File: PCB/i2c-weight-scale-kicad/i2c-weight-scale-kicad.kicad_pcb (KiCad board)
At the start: 2 copper layers, 43 x 49 mm, 13 parts, among them J1 I2C_RJ14, P1 4_STRAIN_GAUGES, U1 INA126, U2 PIC12F1822

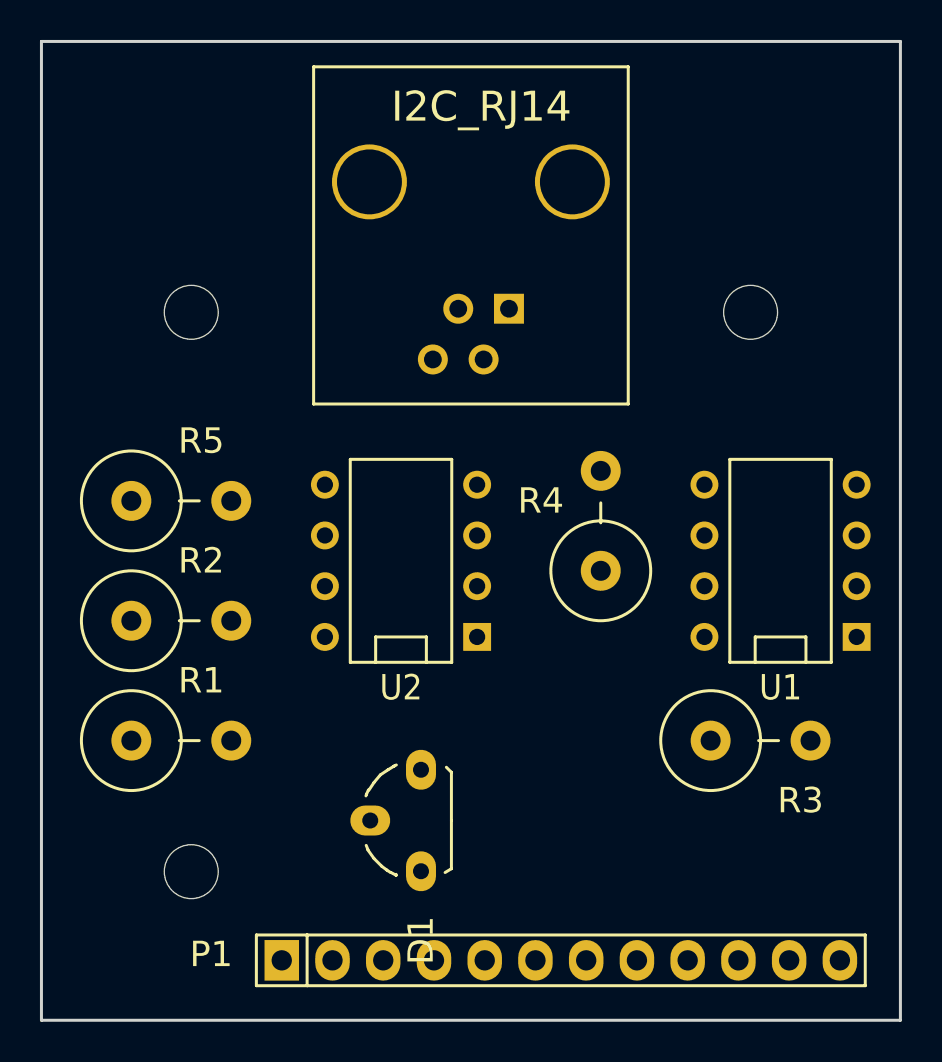
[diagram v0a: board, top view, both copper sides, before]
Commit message: General PCB component placements
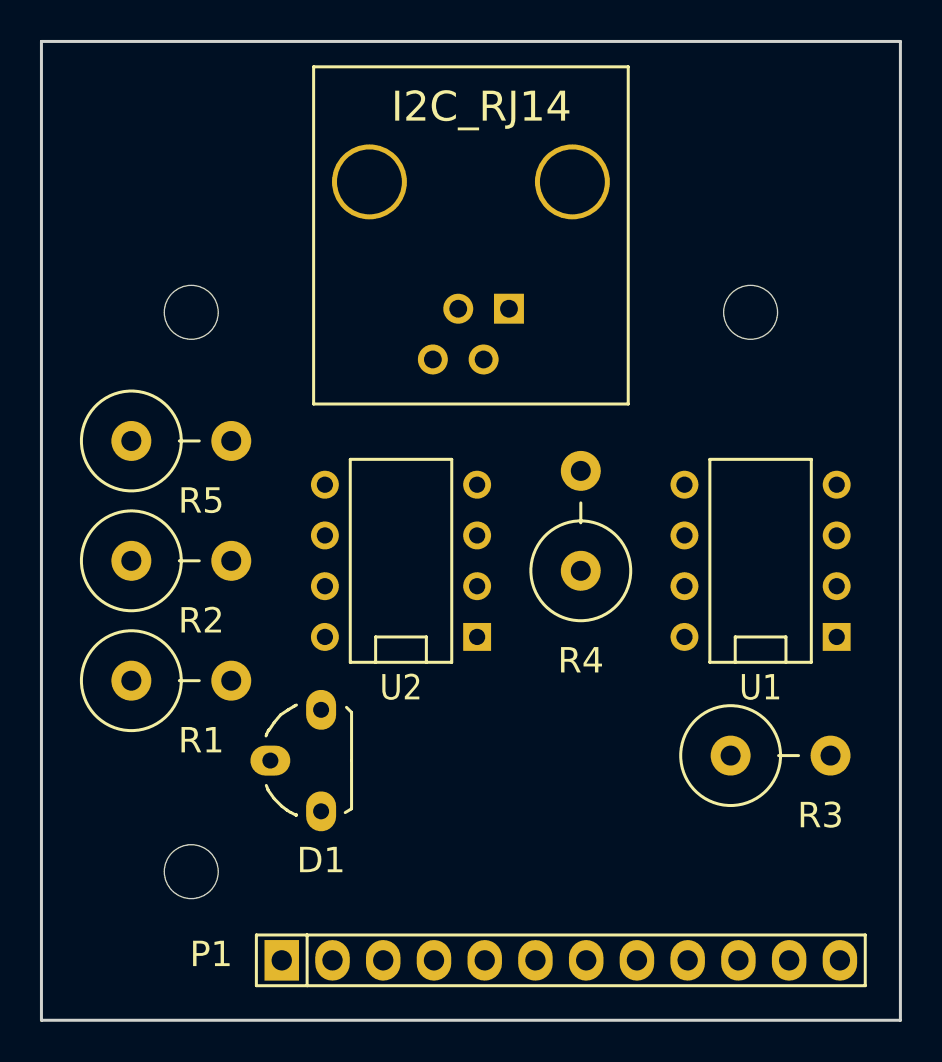
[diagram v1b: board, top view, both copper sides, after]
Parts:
- moved D1 5.83 mm to (64.0, 86.0)
- moved R1 3.00 mm to (57.0, 82.0)
- moved R2 3.00 mm to (57.0, 76.0)
- moved R5 3.00 mm to (57.0, 70.0)
- moved R3 1.25 mm to (87.0, 85.8)
- moved R4 1.00 mm to (77.0, 74.0)
- moved U1 1.00 mm to (86.0, 76.0)
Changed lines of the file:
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@@
     (links 26)
     (no_connects 26)
-    (area 31.86523 49.924999 111.33289 130.184001)
+    (area 31.86523 49.924999 111.33289 99.075001)
     (thickness 1.6)
     (drawings 4)
@@
   )
   (module Housings_TO-92:TO-92-Free-molded-wide-oval (layer F.Cu)
-    (at 69 89 180)
+    (at 64 86 180)
     (descr "TO-92 allgemein free molded wide oval drill 0,8mm")
     (tags "TO-92 allgemein free molded wide oval drill 0,8mm")
-    (fp_text reference D1 (at 0 -6 270) (layer F.SilkS)
+    (fp_text reference D1 (at 0 -5 360) (layer F.SilkS)
       (effects (font (thickness 0.3048)))
     )
@@
   )
   (module Resistors_ThroughHole:Resistor_Vertical_RM5mm (layer F.Cu)
-    (at 57 85)
-    (descr "Resistor, Vertical, RM 5mm, 1/3W,")
-    (tags "Resistor, Vertical, RM 5mm, 1/3W,")
-    (fp_text reference R1 (at 1 -3) (layer F.SilkS)
+    (at 57 82)
+    (descr "Resistor, Vertical, RM 5mm, 1/3W,")
+    (tags "Resistor, Vertical, RM 5mm, 1/3W,")
+    (fp_text reference R1 (at 1 3) (layer F.SilkS)
       (effects (font (thickness 0.3048)))
     )
@@
   )
   (module Resistors_ThroughHole:Resistor_Vertical_RM5mm (layer F.Cu)
-    (at 57 79)
-    (descr "Resistor, Vertical, RM 5mm, 1/3W,")
-    (tags "Resistor, Vertical, RM 5mm, 1/3W,")
-    (fp_text reference R2 (at 1 -3) (layer F.SilkS)
+    (at 57 76)
+    (descr "Resistor, Vertical, RM 5mm, 1/3W,")
+    (tags "Resistor, Vertical, RM 5mm, 1/3W,")
+    (fp_text reference R2 (at 1 3) (layer F.SilkS)
       (effects (font (thickness 0.3048)))
     )
@@
   )
   (module Resistors_ThroughHole:Resistor_Vertical_RM5mm (layer F.Cu)
-    (at 86 85)
+    (at 87 85.75)
     (descr "Resistor, Vertical, RM 5mm, 1/3W,")
     (tags "Resistor, Vertical, RM 5mm, 1/3W,")
@@
   )
   (module Resistors_ThroughHole:Resistor_Vertical_RM5mm (layer F.Cu)
-    (at 78 74 90)
-    (descr "Resistor, Vertical, RM 5mm, 1/3W,")
-    (tags "Resistor, Vertical, RM 5mm, 1/3W,")
-    (fp_text reference R4 (at 1 -3 180) (layer F.SilkS)
+    (at 77 74 90)
+    (descr "Resistor, Vertical, RM 5mm, 1/3W,")
+    (tags "Resistor, Vertical, RM 5mm, 1/3W,")
+    (fp_text reference R4 (at -7 0 180) (layer F.SilkS)
       (effects (font (thickness 0.3048)))
     )
@@
   )
   (module Resistors_ThroughHole:Resistor_Vertical_RM5mm (layer F.Cu)
-    (at 57 73)
-    (descr "Resistor, Vertical, RM 5mm, 1/3W,")
-    (tags "Resistor, Vertical, RM 5mm, 1/3W,")
-    (fp_text reference R5 (at 1 -3) (layer F.SilkS)
+    (at 57 70)
+    (descr "Resistor, Vertical, RM 5mm, 1/3W,")
+    (tags "Resistor, Vertical, RM 5mm, 1/3W,")
+    (fp_text reference R5 (at 1 3) (layer F.SilkS)
       (effects (font (thickness 0.3048)))
     )
@@
   )
   (module Sockets_DIP:DIP-8__300 (layer F.Cu)
-    (at 87 76 90)
+    (at 86 76 90)
     (descr "8 pins DIL package, round pads")
     (tags DIL)

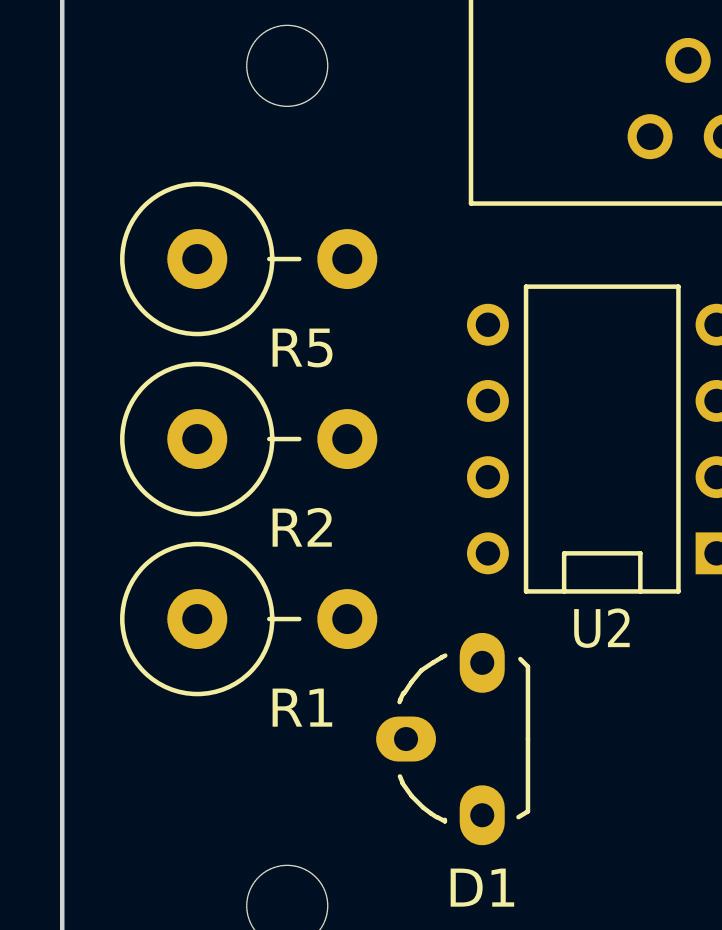
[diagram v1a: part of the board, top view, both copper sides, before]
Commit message: Smarter resistor placement
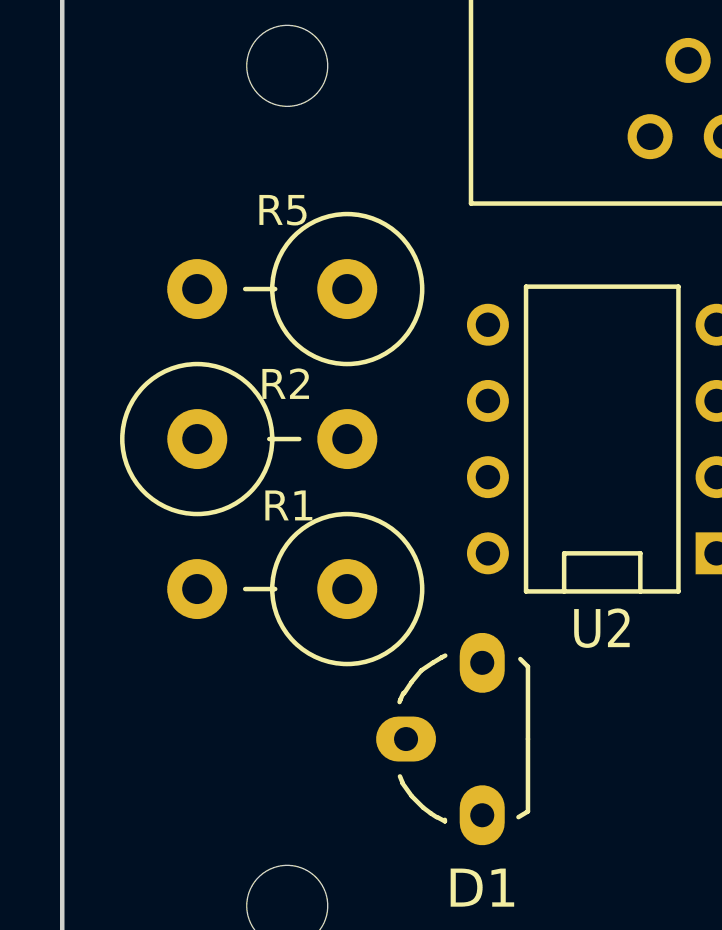
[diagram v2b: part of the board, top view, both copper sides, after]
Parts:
- moved R1 1.00 mm to (57.0, 81.0), turned to 180 degrees
- moved R5 1.00 mm to (57.0, 71.0), turned to 180 degrees
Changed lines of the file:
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@@
   )
   (module Resistors_ThroughHole:Resistor_Vertical_RM5mm (layer F.Cu)
-    (at 57 82)
+    (at 57 81 180)
     (descr "Resistor, Vertical, RM 5mm, 1/3W,")
     (tags "Resistor, Vertical, RM 5mm, 1/3W,")
-    (fp_text reference R1 (at 1 3) (layer F.SilkS)
-      (effects (font (thickness 0.3048)))
+    (fp_text reference R1 (at -0.55 2.75 180) (layer F.SilkS)
+      (effects (font (size 1 1) (thickness 0.2)))
     )
-    (fp_text value 1K5 (at 0 4.50088) (layer F.SilkS) hide
+    (fp_text value 1K5 (at 0 4.50088 180) (layer F.SilkS) hide
       (effects (font (size 1.50114 1.50114) (thickness 0.20066)))
     )
     (fp_line (start -0.09906 0) (end 0.9017 0) (layer F.SilkS) (width 0.15))
     (fp_circle (center -2.49936 0) (end 0 0) (layer F.SilkS) (width 0.15))
-    (pad 1 thru_hole circle (at -2.49936 0) (size 1.99898 1.99898) (drill 1.00076) (layers *.Cu *.SilkS *.Mask)
+    (pad 1 thru_hole circle (at -2.49936 0 180) (size 1.99898 1.99898) (drill 1.00076) (layers *.Cu *.SilkS *.Mask)
       (net 13 "Net-(R1-Pad1)"))
-    (pad 2 thru_hole circle (at 2.5019 0) (size 1.99898 1.99898) (drill 1.00076) (layers *.Cu *.SilkS *.Mask)
+    (pad 2 thru_hole circle (at 2.5019 0 180) (size 1.99898 1.99898) (drill 1.00076) (layers *.Cu *.SilkS *.Mask)
       (net 1 "Net-(D1-Pad2)"))
   )
@@
     (descr "Resistor, Vertical, RM 5mm, 1/3W,")
     (tags "Resistor, Vertical, RM 5mm, 1/3W,")
-    (fp_text reference R2 (at 1 3) (layer F.SilkS)
-      (effects (font (thickness 0.3048)))
+    (fp_text reference R2 (at 0.45 -1.8) (layer F.SilkS)
+      (effects (font (size 1 1) (thickness 0.2)))
     )
     (fp_text value 1K (at 0 4.50088) (layer F.SilkS) hide
@@
   )
   (module Resistors_ThroughHole:Resistor_Vertical_RM5mm (layer F.Cu)
-    (at 57 70)
+    (at 57 71 180)
     (descr "Resistor, Vertical, RM 5mm, 1/3W,")
     (tags "Resistor, Vertical, RM 5mm, 1/3W,")
-    (fp_text reference R5 (at 1 3) (layer F.SilkS)
-      (effects (font (thickness 0.3048)))
+    (fp_text reference R5 (at -0.35 2.6 180) (layer F.SilkS)
+      (effects (font (size 1 1) (thickness 0.2)))
     )
-    (fp_text value 10K (at 0 4.50088) (layer F.SilkS) hide
+    (fp_text value 10K (at 0 4.50088 180) (layer F.SilkS) hide
       (effects (font (size 1.50114 1.50114) (thickness 0.20066)))
     )
     (fp_line (start -0.09906 0) (end 0.9017 0) (layer F.SilkS) (width 0.15))
     (fp_circle (center -2.49936 0) (end 0 0) (layer F.SilkS) (width 0.15))
-    (pad 1 thru_hole circle (at -2.49936 0) (size 1.99898 1.99898) (drill 1.00076) (layers *.Cu *.SilkS *.Mask)
+    (pad 1 thru_hole circle (at -2.49936 0 180) (size 1.99898 1.99898) (drill 1.00076) (layers *.Cu *.SilkS *.Mask)
       (net 17 "Net-(R5-Pad1)"))
-    (pad 2 thru_hole circle (at 2.5019 0) (size 1.99898 1.99898) (drill 1.00076) (layers *.Cu *.SilkS *.Mask)
+    (pad 2 thru_hole circle (at 2.5019 0 180) (size 1.99898 1.99898) (drill 1.00076) (layers *.Cu *.SilkS *.Mask)
       (net 6 VDD))
   )

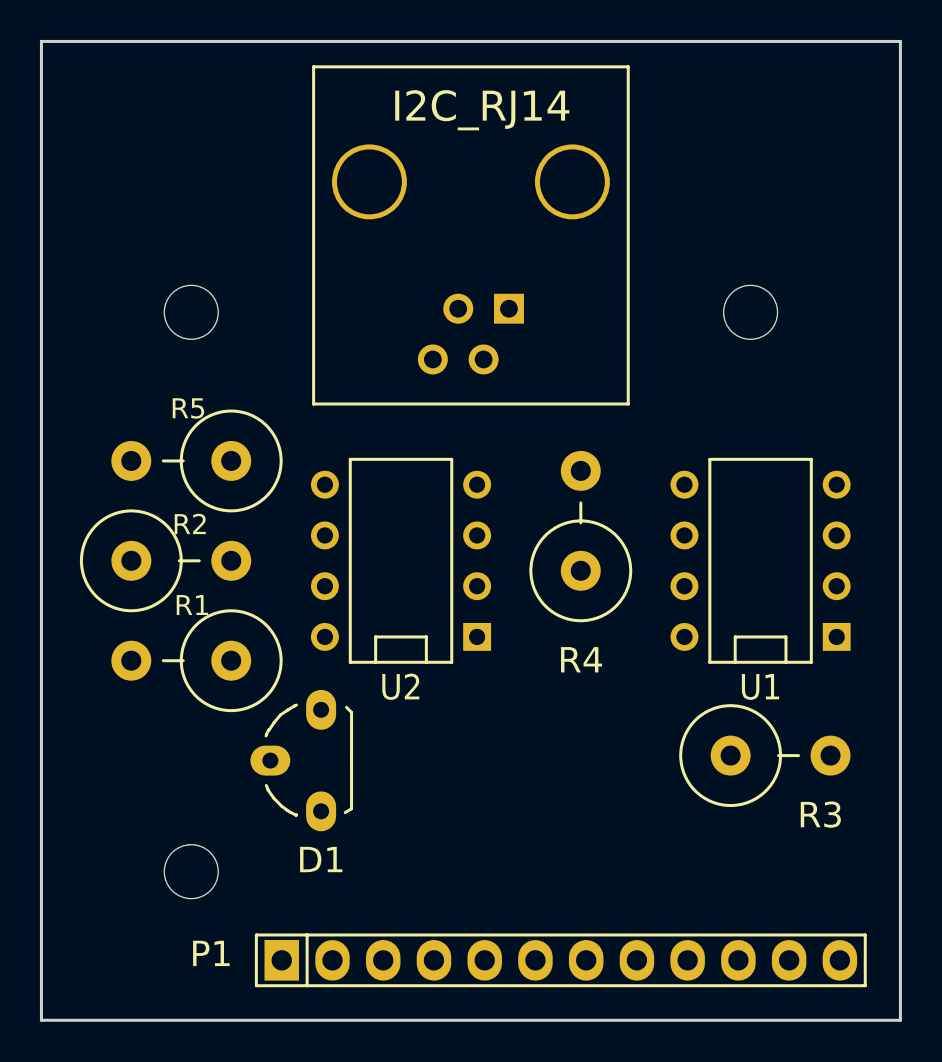
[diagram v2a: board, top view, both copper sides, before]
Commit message: Strain gauge connector traces done
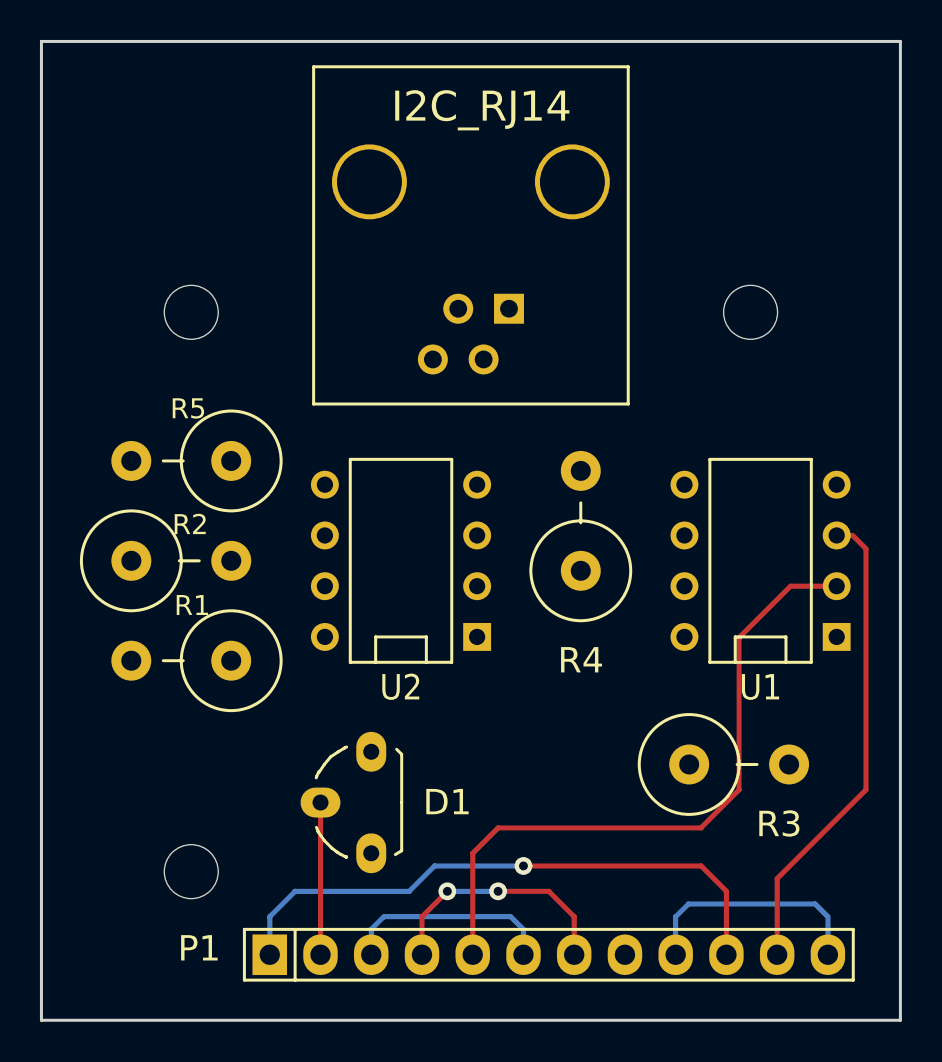
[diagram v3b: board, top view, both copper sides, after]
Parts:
- moved D1 3.27 mm to (66.5, 88.1)
- moved R3 2.12 mm to (84.9, 86.2)
- moved P1 0.66 mm to (75.4, 95.7)
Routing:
- net Net-(P1-Pad5): track 0.00 -> 33.3 mm
- net Net-(P1-Pad1): track 0.00 -> 29.5 mm, vias 0 -> 1
- net Net-(P1-Pad11): track 0.00 -> 23.9 mm
- net Net-(P1-Pad4): track 0.00 -> 12.5 mm, vias 0 -> 2
- net Net-(P1-Pad12): track 0.00 -> 12.0 mm
- net Net-(P1-Pad3): track 0.00 -> 10.7 mm
- net Net-(D1-Pad2): track 0.00 -> 7.62 mm
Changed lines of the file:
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@@
   (general
     (links 26)
-    (no_connects 26)
+    (no_connects 19)
     (area 31.86523 49.924999 111.33289 99.075001)
     (thickness 1.6)
     (drawings 4)
-    (tracks 0)
+    (tracks 40)
     (zones 0)
     (modules 13)
@@
   )
   (module Housings_TO-92:TO-92-Free-molded-wide-oval (layer F.Cu)
-    (at 64 86 180)
+    (at 66.51 88.1 180)
     (descr "TO-92 allgemein free molded wide oval drill 0,8mm")
     (tags "TO-92 allgemein free molded wide oval drill 0,8mm")
-    (fp_text reference D1 (at 0 -5 360) (layer F.SilkS)
+    (fp_text reference D1 (at -3.81 0 360) (layer F.SilkS)
       (effects (font (thickness 0.3048)))
     )
@@
   )
   (module Pin_Headers:Pin_Header_Straight_1x12 (layer F.Cu)
-    (at 76 96)
+    (at 75.4 95.72)
     (descr "Through hole pin header")
     (tags "pin header")
@@
   )
   (module Resistors_ThroughHole:Resistor_Vertical_RM5mm (layer F.Cu)
-    (at 87 85.75)
+    (at 84.925 86.195)
     (descr "Resistor, Vertical, RM 5mm, 1/3W,")
     (tags "Resistor, Vertical, RM 5mm, 1/3W,")
@@
   (gr_line (start 93 50) (end 93 99) (angle 90) (layer Edge.Cuts) (width 0.15))
   (gr_line (start 50 50) (end 93 50) (angle 90) (layer Edge.Cuts) (width 0.15))
+  (segment (start 63.97 95.72) (end 63.97 88.1) (width 0.254) (layer F.Cu) (net 1) (status C00000))
+  (segment (start 61.43 95.72) (end 61.43 93.815) (width 0.254) (layer B.Cu) (net 7) (status 400000))
+  (segment (start 84.29 92.545) (end 84.29 95.72) (width 0.254) (layer F.Cu) (net 7) (status 800000))
+  (segment (start 83.02 91.275) (end 84.29 92.545) (width 0.254) (layer F.Cu) (net 7))
+  (segment (start 74.13 91.275) (end 83.02 91.275) (width 0.254) (layer F.Cu) (net 7))
+  (via (at 74.13 91.275) (size 0.889) (layers F.Cu B.Cu) (net 7))
+  (segment (start 69.685 91.275) (end 74.13 91.275) (width 0.254) (layer B.Cu) (net 7))
+  (segment (start 68.415 92.545) (end 69.685 91.275) (width 0.254) (layer B.Cu) (net 7))
+  (segment (start 62.7 92.545) (end 68.415 92.545) (width 0.254) (layer B.Cu) (net 7))
+  (segment (start 61.43 93.815) (end 62.7 92.545) (width 0.254) (layer B.Cu) (net 7))
+  (segment (start 66.51 95.72) (end 66.51 94.45) (width 0.254) (layer B.Cu) (net 8) (status 400000))
+  (segment (start 74.13 94.45) (end 74.13 95.72) (width 0.254) (layer B.Cu) (net 8) (status 800000))
+  (segment (start 73.495 93.815) (end 74.13 94.45) (width 0.254) (layer B.Cu) (net 8))
+  (segment (start 67.145 93.815) (end 73.495 93.815) (width 0.254) (layer B.Cu) (net 8))
+  (segment (start 66.51 94.45) (end 67.145 93.815) (width 0.254) (layer B.Cu) (net 8))
+  (segment (start 69.05 95.72) (end 69.05 93.815) (width 0.254) (layer F.Cu) (net 9) (status 400000))
+  (segment (start 76.67 93.815) (end 76.67 95.72) (width 0.254) (layer F.Cu) (net 9) (status 800000))
+  (segment (start 75.4 92.545) (end 76.67 93.815) (width 0.254) (layer F.Cu) (net 9))
+  (segment (start 72.86 92.545) (end 75.4 92.545) (width 0.254) (layer F.Cu) (net 9))
+  (via (at 72.86 92.545) (size 0.889) (layers F.Cu B.Cu) (net 9))
+  (segment (start 70.32 92.545) (end 72.86 92.545) (width 0.254) (layer B.Cu) (net 9))
+  (via (at 70.32 92.545) (size 0.889) (layers F.Cu B.Cu) (net 9))
+  (segment (start 69.05 93.815) (end 70.32 92.545) (width 0.254) (layer F.Cu) (net 9))
+  (segment (start 89.81 77.27) (end 87.5 77.27) (width 0.254) (layer F.Cu) (net 10) (status 400000))
+  (segment (start 71.59 90.64) (end 71.59 95.72) (width 0.254) (layer F.Cu) (net 10) (status 800000))
+  (segment (start 72.86 89.37) (end 71.59 90.64) (width 0.254) (layer F.Cu) (net 10))
+  (segment (start 83.02 89.37) (end 72.86 89.37) (width 0.254) (layer F.Cu) (net 10))
+  (segment (start 84.925 87.465) (end 83.02 89.37) (width 0.254) (layer F.Cu) (net 10))
+  (segment (start 84.925 79.845) (end 84.925 87.465) (width 0.254) (layer F.Cu) (net 10))
+  (segment (start 87.5 77.27) (end 84.925 79.845) (width 0.254) (layer F.Cu) (net 10))
+  (segment (start 81.75 95.72) (end 81.75 93.815) (width 0.254) (layer B.Cu) (net 11) (status 400000))
+  (segment (start 89.37 93.815) (end 89.37 95.72) (width 0.254) (layer B.Cu) (net 11) (status 800000))
+  (segment (start 88.735 93.18) (end 89.37 93.815) (width 0.254) (layer B.Cu) (net 11))
+  (segment (start 82.385 93.18) (end 88.735 93.18) (width 0.254) (layer B.Cu) (net 11))
+  (segment (start 81.75 93.815) (end 82.385 93.18) (width 0.254) (layer B.Cu) (net 11))
+  (segment (start 89.81 74.73) (end 90.605 74.73) (width 0.254) (layer F.Cu) (net 12) (status 400000))
+  (segment (start 86.83 91.91) (end 86.83 95.72) (width 0.254) (layer F.Cu) (net 12) (status 800000))
+  (segment (start 91.275 87.465) (end 86.83 91.91) (width 0.254) (layer F.Cu) (net 12))
+  (segment (start 91.275 75.4) (end 91.275 87.465) (width 0.254) (layer F.Cu) (net 12))
+  (segment (start 90.605 74.73) (end 91.275 75.4) (width 0.254) (layer F.Cu) (net 12))
 )
